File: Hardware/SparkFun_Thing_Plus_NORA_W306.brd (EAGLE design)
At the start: 22.9 x 58.4 mm, 150 parts, among them J1 THING_PLUS_LOGICAL, J2 LiPo, J3 QWIIC_RA, J4 MICRO-SDFRICTION, J5 USB-C, Q1 3.1A/30V/105mΩ, Q2 MBT3904DW1T1, U1 UBLOX_NORA_W306, U3 XC6222B331MR-G, U4 MCP73831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

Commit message: Renamed and updated label to STAT Jumper to JP4
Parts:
- removed U$73: (no value), output:#ST#4
- added U$74: (no value), output:#JP4#0
- renumbered LED1 to JP4
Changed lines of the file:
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@@
 <setting verticaltext="up"/>
 </settings>
-<grid distance="0.05" unitdist="inch" unit="inch" style="lines" multiple="1" display="yes" altdistance="0.005" altunitdist="inch" altunit="inch"/>
+<grid distance="0.05" unitdist="inch" unit="inch" style="lines" multiple="1" display="yes" altdistance="0.0001" altunitdist="inch" altunit="inch"/>
 <layers>
 <layer number="1" name="Top" color="4" fill="1" visible="yes" active="yes"/>
@@
 <dimension x1="2.54" y1="2.54" x2="0" y2="2.54" x3="1.27" y3="-5.08" textsize="1.016" textratio="10" layer="47" width="0.0762" unit="inch"/>
 <dimension x1="20.32" y1="2.54" x2="22.86" y2="2.54" x3="21.59" y3="-5.08" textsize="1.016" textratio="10" layer="47" width="0.0762" unit="inch"/>
-<dimension x1="22.86" y1="2.54" x2="0" y2="2.54" x3="11.43" y3="-12.7" textsize="1.016" textratio="10" layer="47" width="0.0762" unit="inch" visible="yes"/>
-<dimension x1="2.54" y1="0" x2="2.54" y2="58.42" x3="-30.48" y3="29.21" textsize="1.016" textratio="10" layer="47" width="0.0762" unit="inch"/>
+<dimension x1="22.86" y1="2.54" x2="0" y2="2.54" x3="11.43" y3="-12.7" textsize="1.016" textratio="10" layer="47" width="0.0762" unit="inch"/>
+<dimension x1="2.54" y1="0" x2="2.54" y2="58.42" x3="-26.67" y3="29.21" textsize="1.016" textratio="10" layer="47" width="0.0762" unit="inch"/>
 <text x="-5.08" y="-22.86" size="1.778" layer="51" font="vector">Based on designs by: M. Hord, A. Wende</text>
 <wire x1="10.34541875" y1="26.863046875" x2="10.4673375" y2="27.005284375" width="0.2032" layer="22"/>
@@
 </element>
 <element name="U$72" library="output" package="#I2C#3" value="" x="2.999740625" y="7.67588125" smashed="yes" rot="MR90"/>
-<element name="LED1" library="SparkFun-Jumpers" package="SMT-JUMPER_2_NC_TRACE_SILK" package3d_urn="urn:adsk.eagle:package:39281/1" value="" x="5.7658" y="33.825178125" smashed="yes" rot="MR90">
+<element name="JP4" library="SparkFun-Jumpers" package="SMT-JUMPER_2_NC_TRACE_SILK" package3d_urn="urn:adsk.eagle:package:39281/1" value="" x="5.7658" y="33.825178125" smashed="yes" rot="MR90">
 <attribute name="NAME" x="6.9088" y="33.825178125" size="0.6096" layer="26" font="vector" ratio="20" rot="MR90" align="bottom-center"/>
 <attribute name="VALUE" x="4.6228" y="33.825178125" size="0.6096" layer="28" font="vector" ratio="20" rot="MR90" align="top-center"/>
 </element>
-<element name="U$73" library="output" package="#ST#4" value="" x="5.7937375" y="31.53918125" smashed="yes" rot="MR90"/>
 <element name="C11" library="SparkFun-Capacitors" package="0402-TIGHT" value="0.1uF" x="21.59" y="9.017" smashed="yes" rot="R270">
 <attribute name="NAME" x="22.352" y="9.017" size="0.6096" layer="25" font="vector" ratio="20" rot="R270" align="bottom-center"/>
@@
 <attribute name="VALUE" x="20.828" y="9.017" size="0.6096" layer="27" font="vector" ratio="20" rot="R270" align="top-center"/>
 </element>
+<element name="U$74" library="output" package="#JP4#0" value="" x="5.78611875" y="31.480759375" smashed="yes" rot="MR90"/>
 </elements>
 <signals>
@@
 <wire x1="6.36778125" y1="42.53738125" x2="5.69721875" y2="41.86681875" width="0.1778" layer="1"/>
 <wire x1="4.472940625" y1="41.0057625" x2="4.472940625" y2="37.492940625" width="0.1778" layer="1"/>
-<contactref element="LED1" pad="1"/>
+<contactref element="JP4" pad="1"/>
 <wire x1="3.754121875" y1="34.29" x2="4.75488125" y2="33.289240625" width="0.1778" layer="1"/>
 <via x="4.75488125" y="33.289240625" extent="1-16" drill="0.254"/>
@@
 <signal name="N$22">
 <contactref element="R4" pad="1"/>
-<contactref element="LED1" pad="2"/>
+<contactref element="JP4" pad="2"/>
 <wire x1="5.7658" y1="34.345878125" x2="6.58368125" y2="34.345878125" width="0.1778" layer="16"/>
 <wire x1="6.58368125" y1="34.345878125" x2="7.152640625" y2="33.77691875" width="0.1778" layer="16"/>

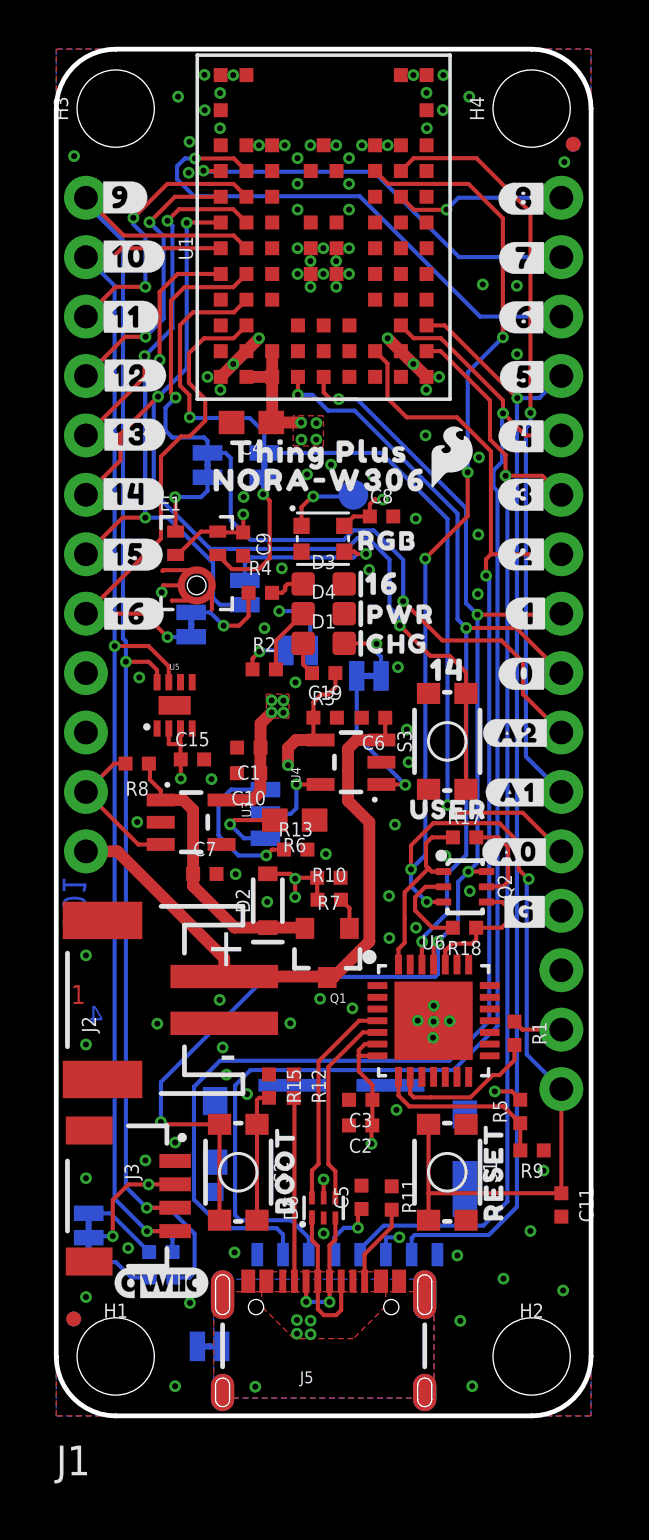
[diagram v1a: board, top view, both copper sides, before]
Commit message: Switched to SPI1 and alternate TX1/RX1 pins
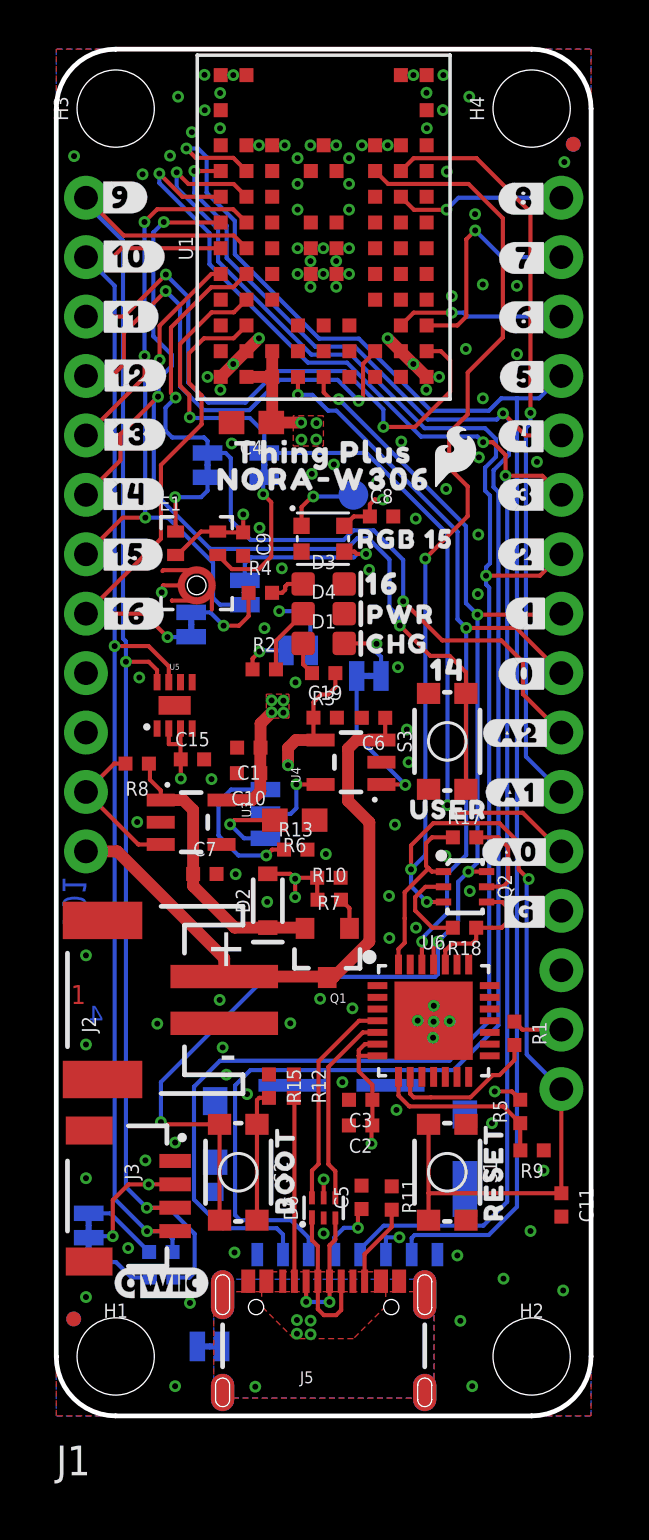
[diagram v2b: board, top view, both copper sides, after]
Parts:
- removed U$9: (no value), output:RGB0
- added U$73: (no value), output:RGB_155
- moved U$62 0.18 mm to (11.6, 41.2)
- moved U$5 0.18 mm to (11.4, 40.0)
- moved U$8 0.15 mm to (17.0, 41.0)
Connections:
- removed net PA12/LP_UART_TXD: J1.14, U1.J9
- removed net PA13/LP_UART_RXD: J1.15, U1.J8
- removed net PA14: J1.4, U1.H9
- removed net PA15: J1.3, U1.H8
- removed net PA25/PICO: J1.17, J4.3, U1.C2
- removed net PA26/POCI: J1.16, J4.7, U1.C1
- removed net PA28/CS: J1.19, J4.2, U1.B3
- removed net PA30/SCK: J1.18, J4.5, U1.B1
- new net PA12/PICO: J1.17, J4.3, U1.J9
- new net PA13/POCI: J1.16, J4.7, U1.J8
- new net PA14/SCK: J1.18, J4.5, U1.H9
- new net PA15/CS: J1.19, J4.2, U1.H8
- new net PA25/LP_UART_RXD: J1.15, U1.C2
- new net PA26/LP_UART_TXD: J1.14, U1.C1
- new net PA28: J1.4, U1.B3
- new net PA30: J1.3, U1.B1
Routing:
- net PA15/CS: track 0.00 -> 75.7 mm, vias 0 -> 2
- net PA12/PICO: track 0.00 -> 71.8 mm, vias 0 -> 2
- net PA13/POCI: track 0.00 -> 66.3 mm, vias 0 -> 1
- net PA14/SCK: track 0.00 -> 65.9 mm, vias 0 -> 3
- net PA28/CS: track 59.0 -> 0.00 mm, vias 1 -> 0
- net PA25/PICO: track 57.6 -> 0.00 mm, vias 1 -> 0
- net PA30/SCK: track 48.2 -> 0.00 mm, vias 1 -> 0
- net PA26/POCI: track 47.8 -> 0.00 mm, vias 1 -> 0
- net PA30: track 0.00 -> 25.8 mm, vias 0 -> 2
- net PA13/LP_UART_RXD: track 22.7 -> 0.00 mm, vias 1 -> 0
- net PA28: track 0.00 -> 21.4 mm, vias 0 -> 2
- net PA12/LP_UART_TXD: track 17.6 -> 0.00 mm, vias 1 -> 0
- net PA14: track 12.2 -> 0.00 mm, vias 2 -> 0
- net PA15: track 11.9 -> 0.00 mm, vias 2 -> 0
- net PA26/LP_UART_TXD: track 0.00 -> 9.85 mm, vias 0 -> 1
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
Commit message: bumping version to v02
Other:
- board text added: "v02"
- board text removed: "v01"
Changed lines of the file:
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@@
 <setting verticaltext="up"/>
 </settings>
-<grid distance="0.05" unitdist="inch" unit="inch" style="lines" multiple="1" display="yes" altdistance="0.0001" altunitdist="inch" altunit="inch"/>
+<grid distance="0.05" unitdist="inch" unit="inch" style="lines" multiple="1" display="yes" altdistance="0.005" altunitdist="inch" altunit="inch"/>
 <layers>
 <layer number="1" name="Top" color="4" fill="1" visible="yes" active="yes"/>
@@
 <layer number="20" name="Dimension" color="24" fill="1" visible="yes" active="yes"/>
 <layer number="21" name="tPlace" color="16" fill="1" visible="yes" active="yes"/>
-<layer number="22" name="bPlace" color="14" fill="1" visible="no" active="yes"/>
+<layer number="22" name="bPlace" color="14" fill="1" visible="yes" active="yes"/>
 <layer number="23" name="tOrigins" color="15" fill="1" visible="yes" active="yes"/>
-<layer number="24" name="bOrigins" color="15" fill="1" visible="no" active="yes"/>
+<layer number="24" name="bOrigins" color="15" fill="1" visible="yes" active="yes"/>
 <layer number="25" name="tNames" color="7" fill="1" visible="no" active="yes"/>
 <layer number="26" name="bNames" color="7" fill="1" visible="no" active="yes"/>
@@
 <layer number="48" name="Document" color="7" fill="1" visible="no" active="yes"/>
 <layer number="49" name="Reference" color="7" fill="1" visible="yes" active="yes"/>
-<layer number="51" name="tDocu" color="6" fill="1" visible="no" active="yes"/>
+<layer number="51" name="tDocu" color="6" fill="1" visible="yes" active="yes"/>
 <layer number="52" name="bDocu" color="7" fill="1" visible="no" active="yes"/>
 <layer number="3" name="Route3" color="4" fill="3" visible="no" active="no"/>
@@
 <wire x1="2.54" y1="0" x2="20.32" y2="0" width="0.2032" layer="20"/>
 <wire x1="20.32" y1="0" x2="22.86" y2="2.54" width="0.2032" layer="20" curve="90"/>
-<text x="0.782321875" y="23.0759" size="1.016" layer="16" font="vector" ratio="20" rot="MR270" align="center-left">v01</text>
+<text x="0.782321875" y="23.0759" size="1.016" layer="16" font="vector" ratio="20" rot="MR270" align="center-left">v02</text>
 <text x="0.6223" y="17.604740625" size="0.8128" layer="1" font="vector" ratio="20">1</text>
 <text x="1.3843" y="17.604740625" size="0.8128" layer="2" font="vector" ratio="20">2</text>

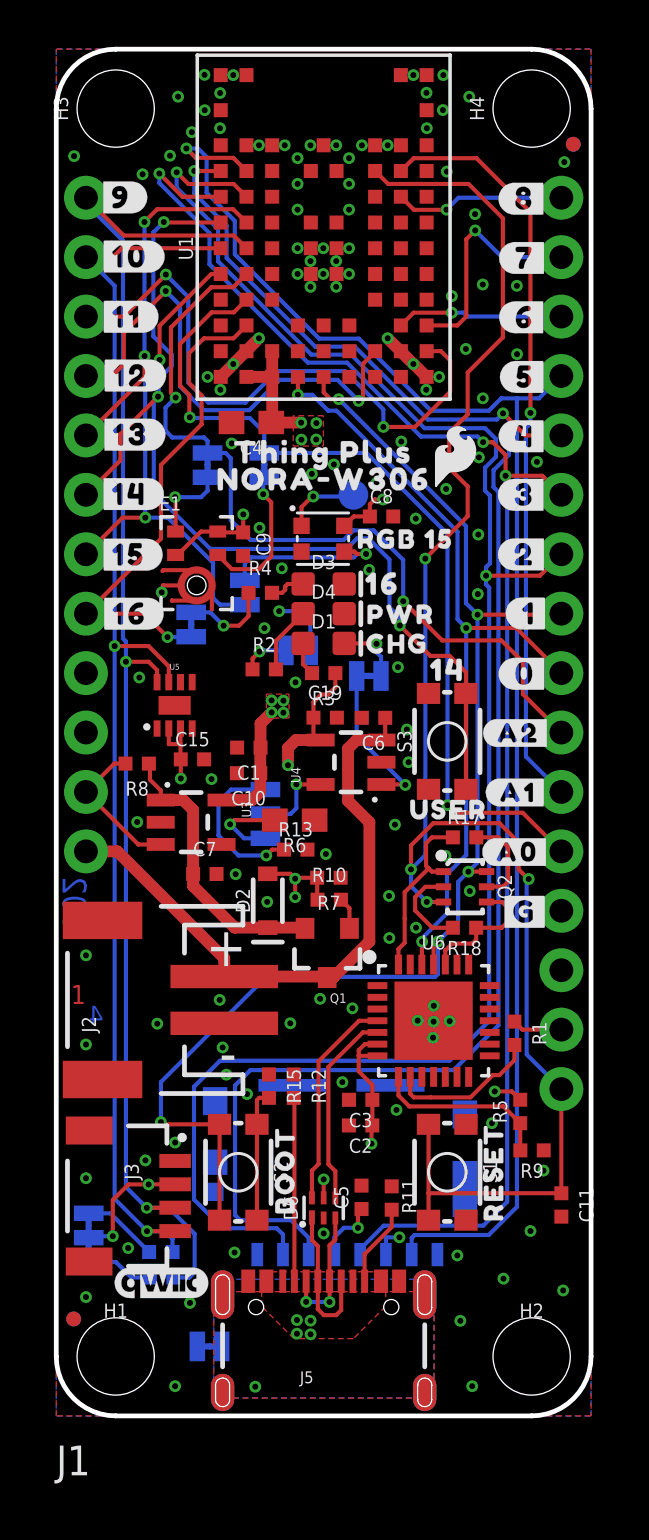
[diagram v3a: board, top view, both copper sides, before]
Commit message: BOM consolidation
-added surface finish instructions (HASL)
-removed layer 100
-all 0.1uF caps are now the same 16V part (there used to be 3 different types).
-all 10uF are now the same part (just changed one cap from 0603 to 0402, but had the same voltage rating).
-all 4.7uF are now 0603, 35V, to accommodate VBATT inputs.
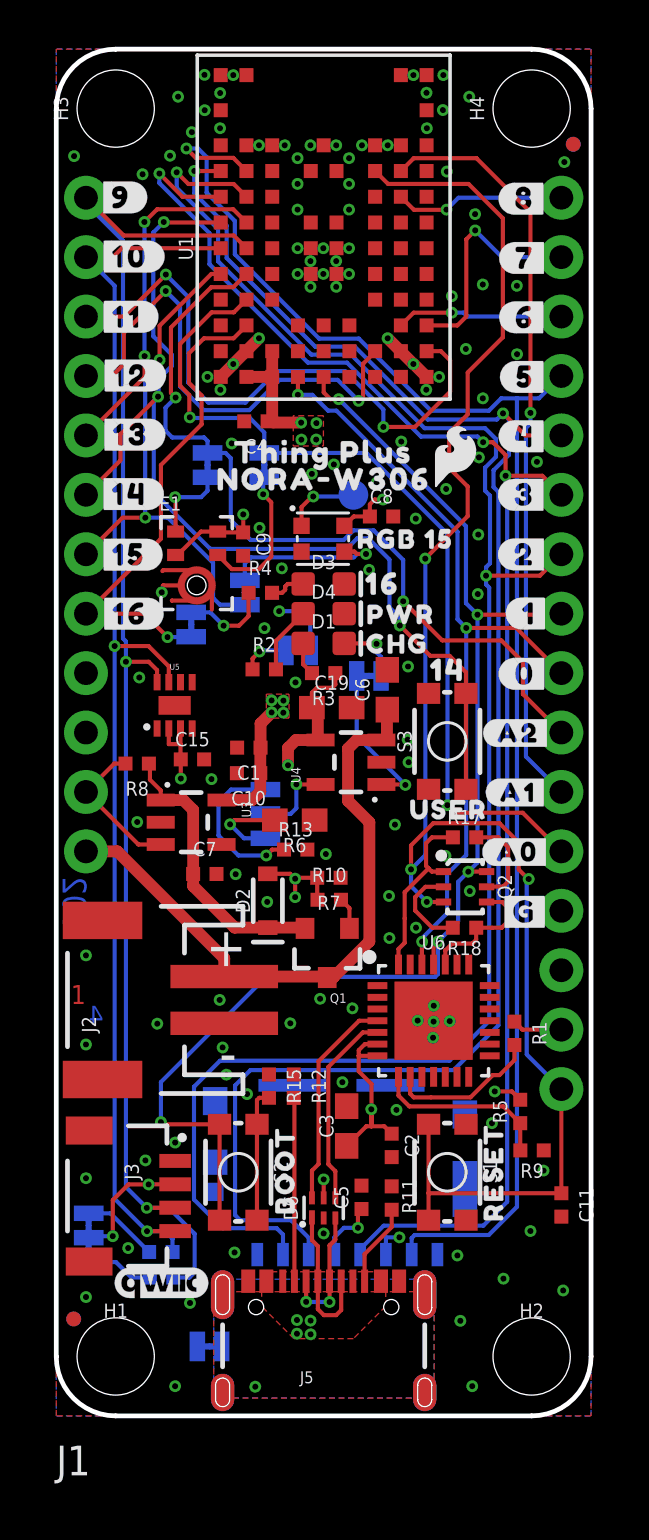
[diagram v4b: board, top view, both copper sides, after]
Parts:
- C19, C3, C6: device SparkFun-Capacitors:0402-TIGHT -> SparkFun-Capacitors:0603
- C4: device SparkFun-Capacitors:0603 -> SparkFun-Capacitors:0402-TIGHT
- moved U$59 12.7 mm to (41.9, 50.8)
- moved C2 1.58 mm to (14.3, 11.6), turned to 270 degrees
- moved C6 1.34 mm to (14.2, 31.0), turned to 90 degrees
- moved C3 1.27 mm to (12.4, 12.4), turned to 90 degrees
- moved C19 0.51 mm to (11.8, 30.3)
- moved C4 0.20 mm to (8.53, 42.5)
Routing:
- net 3.3V: track 45.8 -> 48.4 mm
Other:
- board text added: "Board thickness is 1.6mm 4-Layer 1oz copper outer 0.5oz copper inner Surface Finish: HASL"
- board text removed: "Board thickness is 1.6mm 4-Layer 1oz copper outer 0.5oz copper inner"

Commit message: Added SWD header to bottom side
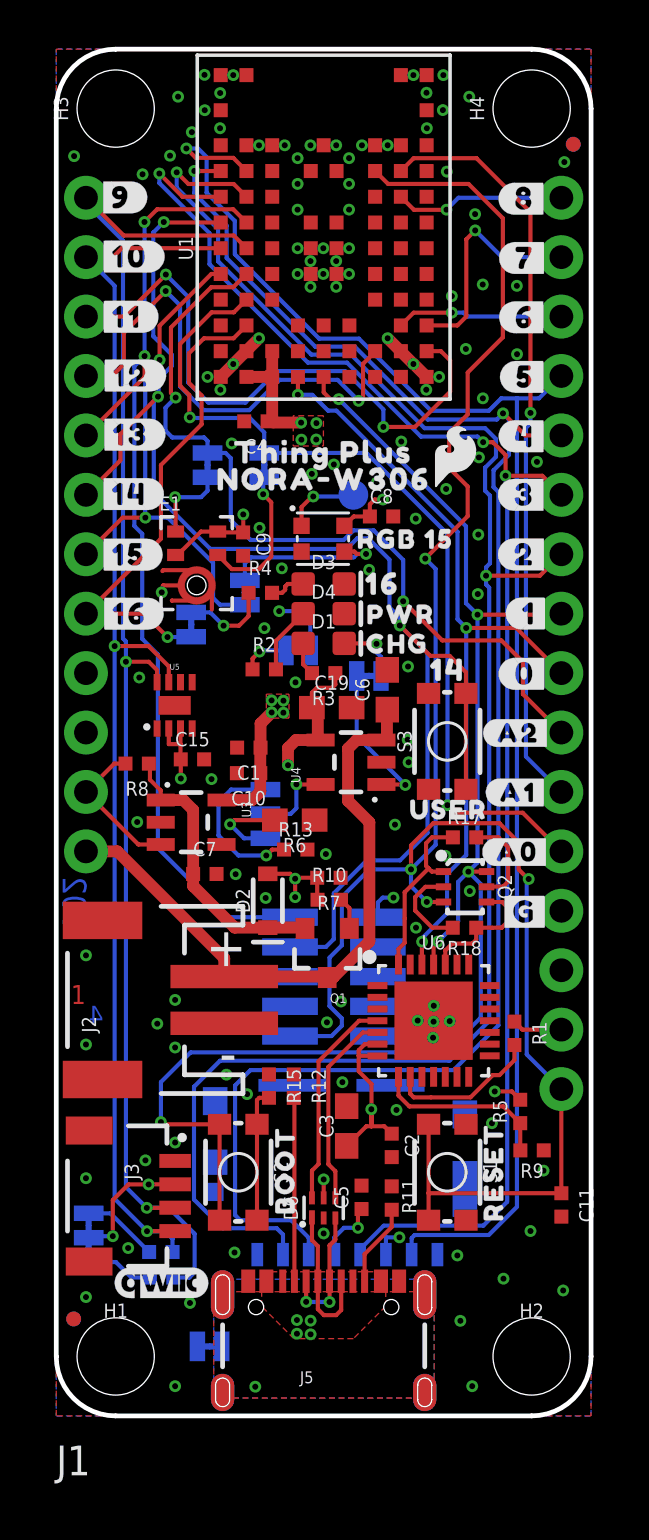
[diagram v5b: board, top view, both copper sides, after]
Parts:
- added J6: SWD, SparkFun-Connectors:2X5-SMD-UNSHROUDED
- added U$9: (no value), output:#500#501
- U$4: device output:#500#0 -> output:#100#501
- U$60: device output:#100#0 -> output:#SWD#501
- moved U$60 8.23 mm to (8.17, 18.8)
- moved LOGO2 7.89 mm to (3.79, 20.3)
- moved U$4 3.67 mm to (8.74, 28.0), turned to 0 degrees
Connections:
- removed net PB18: J1.6, S3.1, S3.2, U1.G9
- removed net PB19: J1.5, U1.G8
- new net PB18/SWD_CL: J1.6, J6.4, S3.1, S3.2, U1.G9
- new net PB19/SWD_DATA: J1.5, J6.2, U1.G8
- net !RESET!: now also J6.10
- net 3.3V: now also J6.1
- net GND: now also J6.3, J6.5, J6.9
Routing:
- net PB18/SWD_CL: track 0.00 -> 62.0 mm, vias 0 -> 3
- net PB18: track 43.6 -> 0.00 mm, vias 3 -> 0
- net PB19/SWD_DATA: track 0.00 -> 43.5 mm, vias 0 -> 2
- net PB19: track 15.0 -> 0.00 mm, vias 2 -> 0
- net !RESET!: track 70.8 -> 82.9 mm
- net PA7/UART-LOG-TXD: track 56.7 -> 62.8 mm
- net 3.3V: track 48.4 -> 49.8 mm, vias 15 -> 16
- net GND: vias 123 -> 120
